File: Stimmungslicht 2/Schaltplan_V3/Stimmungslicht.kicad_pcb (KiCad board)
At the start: 2 copper layers, 37.8 x 37.8 mm, 19 parts, among them IC1 STM32G031J6M6, J1 Conn_01x01, J2 Conn_01x04_Male, U1 HU2032-LF, U101 Touch_Sens_Pad, U102 Touch_Sens_Pad, U103 Touch_Sens_Pad, U104 Touch_Sens_Pad

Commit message: Schaltplan umgesetzt
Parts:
- moved U1 27.0 mm to (143.0, 102.9), turned to 270 degrees
- moved R4 5.83 mm to (140.2, 126.5), turned to 90 degrees
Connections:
- IC1 pad 5: PA8-LEDs -> PA1SendPin-kS
- LED2 pad 1: PA8-LEDs -> Conn-SWDIO
- R3 pad 1: PA8-LEDs -> Conn-SWDIO
- R4 pad 1: Conn-RST -> PA1SendPin-kS
- S1 pad 1: Conn-RST -> PA1SendPin-kS
- U1 pad 1: GND -> +3V3
- U1 pad 2: GND -> +3V3
- U1 pad 3: +3V3 -> GND
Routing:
- net PA1SendPin-kS: track 0.00 -> 38.1 mm
- net Conn-RST: track 38.7 -> 3.90 mm
- net Conn-SWDIO: track 7.87 -> 24.3 mm
- net PA8-LEDs: track 14.2 -> 0.00 mm
- net PA12ReceivePin-kS: track 9.98 -> 11.6 mm

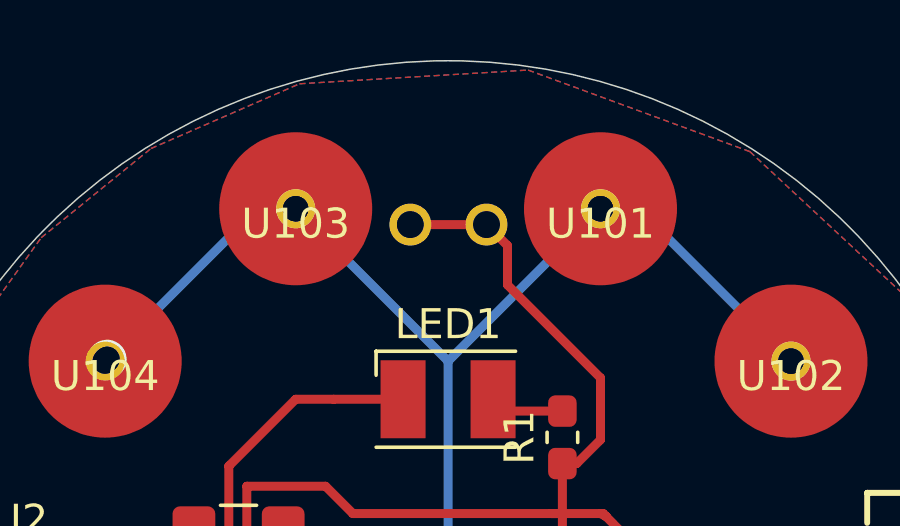
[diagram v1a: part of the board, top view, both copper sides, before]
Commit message: Sensorflaechen angepasst
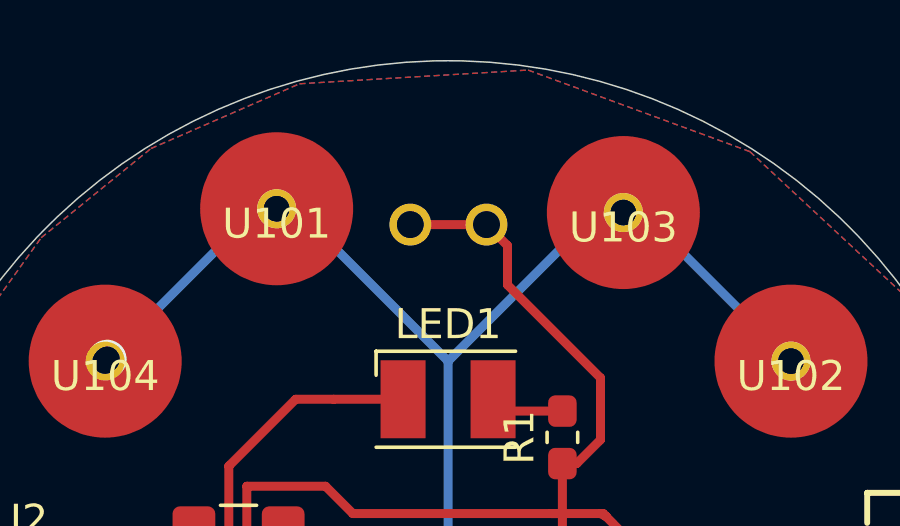
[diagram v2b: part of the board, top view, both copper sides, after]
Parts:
- moved U103 10.9 mm to (150.1, 102.5)
- moved U101 10.8 mm to (138.5, 102.3)

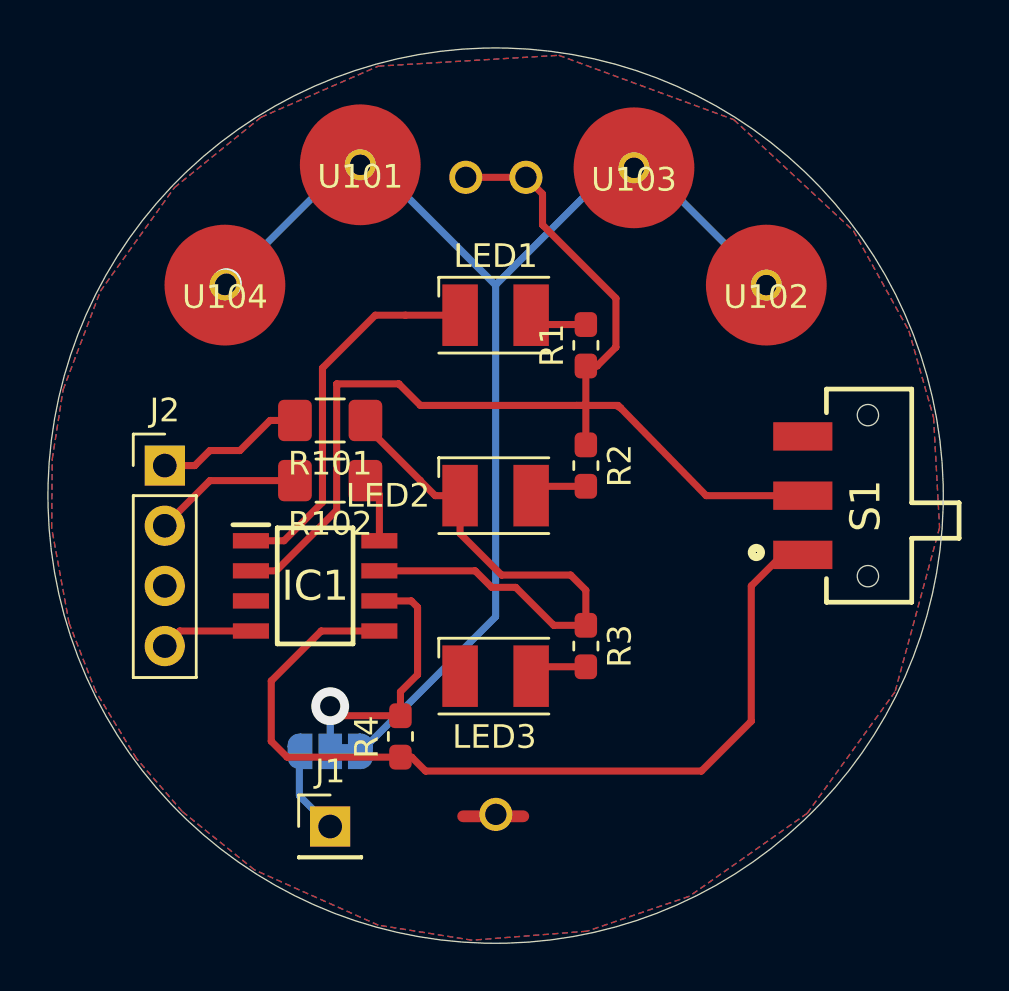
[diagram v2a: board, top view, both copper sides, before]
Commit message: Doppelt Durchführungen entfernt
Einige Warnungen behoben
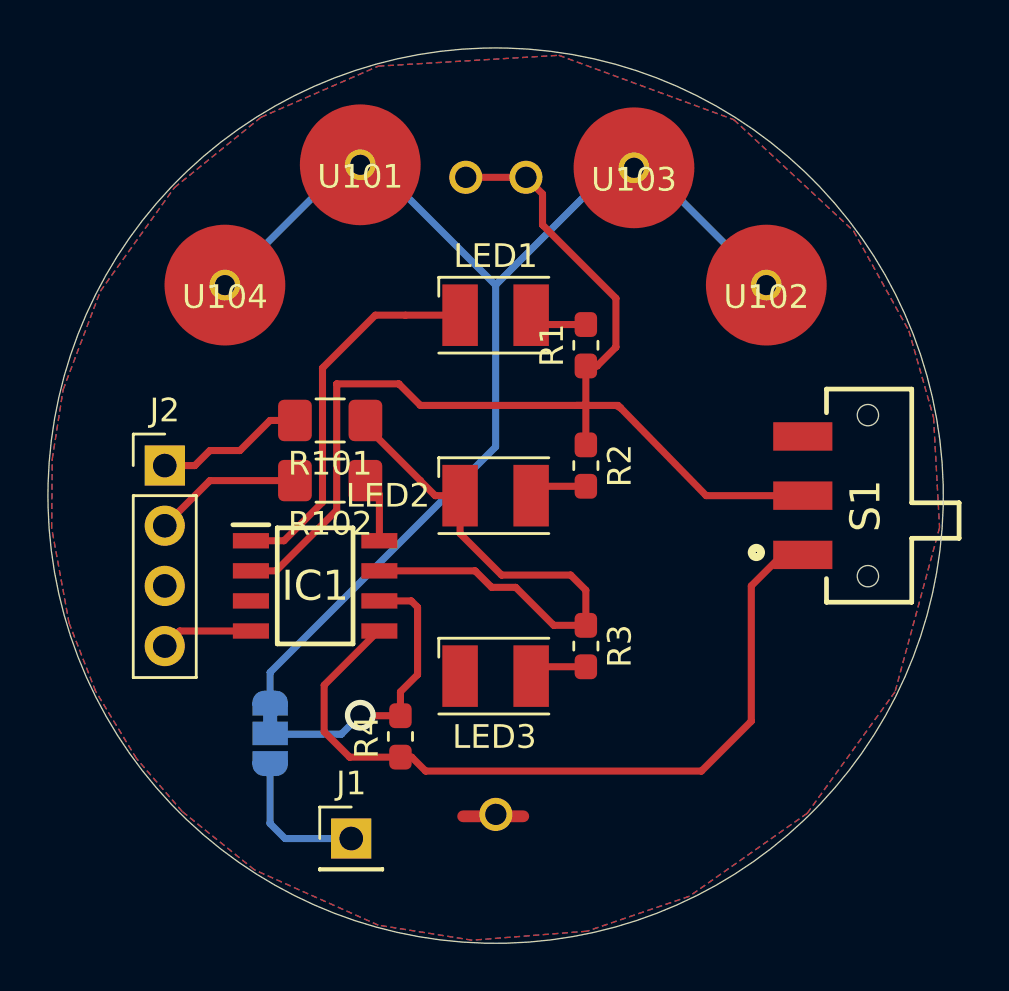
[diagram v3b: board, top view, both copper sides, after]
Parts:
- moved JP101 2.65 mm to (134.7, 126.3), turned to 270 degrees
- moved J1 1.02 mm to (138.1, 130.8)
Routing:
- net PA1SendPin-kS: track 38.1 -> 33.3 mm
- net Net-(J1-Pad1): track 3.71 -> 6.12 mm
- net PA12ReceivePin-kS: track 11.6 -> 12.5 mm
- net Net-(JP101-Pad1): track 53.3 -> 52.8 mm, vias 4 -> 0

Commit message: Aktueller Schaltplan
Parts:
- moved U101 0.11 mm to (138.5, 102.4)
